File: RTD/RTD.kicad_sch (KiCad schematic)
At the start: 48 parts, among them SW1 SW_SPDT, U1 THVD1420D, U2 STM32F103C8Tx

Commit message: light refactor
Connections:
- net -24V: now also SDT1.2 (-VIN); no longer SDT1. (-VIN)
- net 24V: now also SDT1.1 (+VIN); no longer SDT1. (-VIN)
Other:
- moved on the sheet: C1, C4, Debug_power1, Debugger1, F1, L1, L2, Pwr_term1

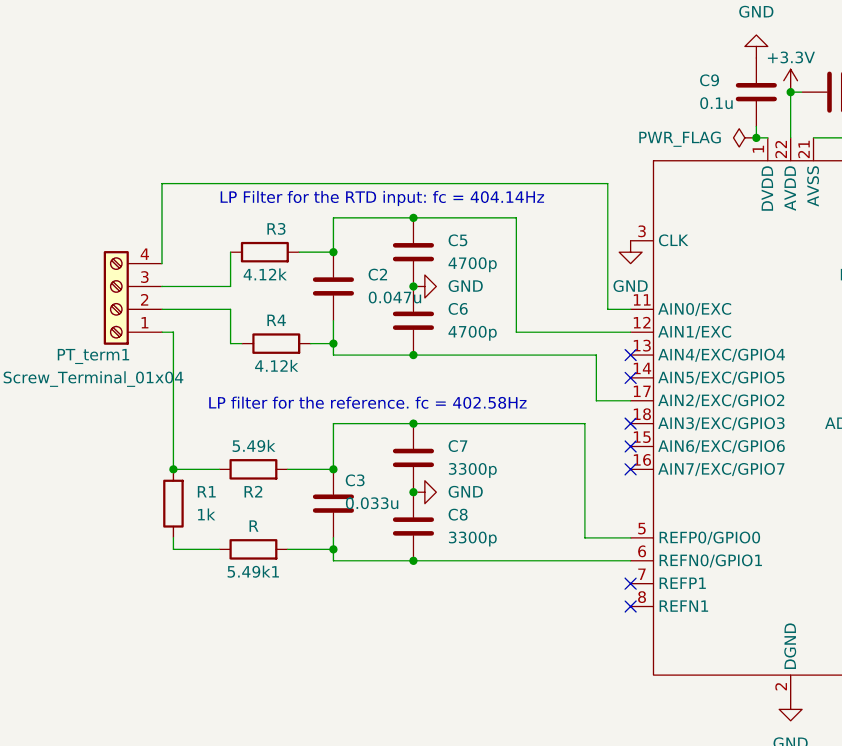
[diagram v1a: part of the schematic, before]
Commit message: fix: changes value in LP filters
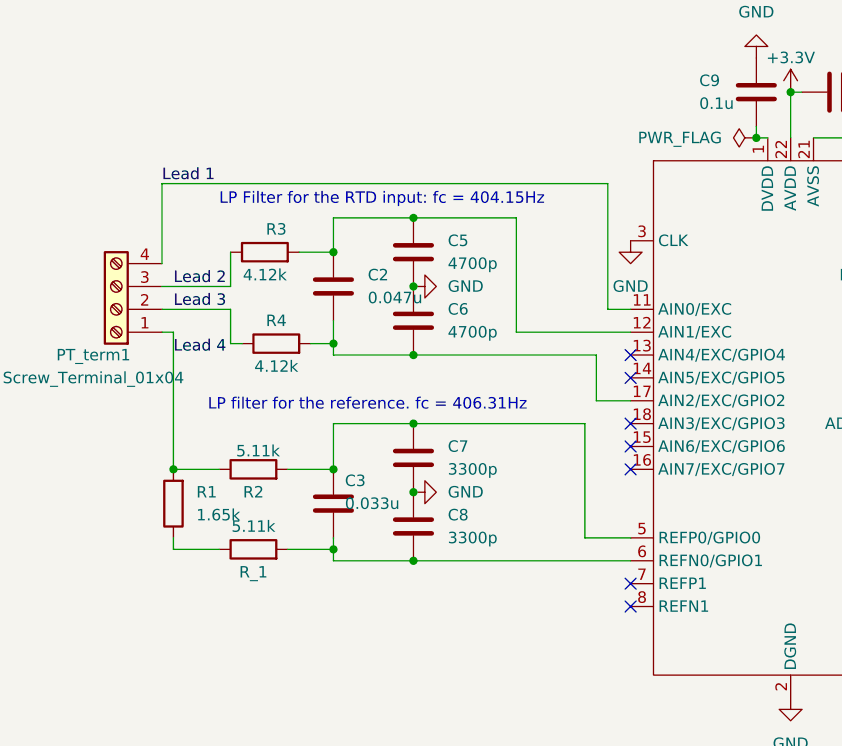
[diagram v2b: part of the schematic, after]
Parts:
- R1: value 1k -> 1.65k
- R2: value 5.49k -> 5.11k
- R_1: renamed from 5.49k1; value R -> 5.11k
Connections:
- net Lead 4: now reaches PT_term1.1 (Pin_1), R1.2, R2.1
- net Lead 3: now reaches PT_term1.2 (Pin_2), R4.1
- net Lead 1: now reaches ADS1.11 (AIN0/EXC), PT_term1.4 (Pin_4)
- net Lead 2: now reaches PT_term1.3 (Pin_3), R3.1
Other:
- note added: "LP Filter for the RTD input: fc = 404.15Hz"
- note added: "LP filter for the reference. fc = 406.31Hz"
- note removed: "LP Filter for the RTD input: fc = 404.14Hz"
- note removed: "LP filter for the reference. fc = 402.58Hz"
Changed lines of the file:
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@@
 		)
 	)
-	(text "LP filter for the reference. fc = 402.58Hz"
+	(text "LP filter for the reference. fc = 406.31Hz"
 		(exclude_from_sim no)
 		(at 43.18 66.04 0)
@@
 		)
 	)
-	(text "LP Filter for the RTD input: fc = 404.14Hz"
+	(text "LP Filter for the RTD input: fc = 404.15Hz"
 		(exclude_from_sim no)
 		(at 44.45 43.18 0)
@@
 		)
 	)
+	(label "Lead 3"
+		(at 39.37 54.61 0)
+		(effects
+			(font
+				(size 1.27 1.27)
+			)
+			(justify left bottom)
+		)
+	)
+	(label "Lead 4"
+		(at 39.37 59.69 0)
+		(effects
+			(font
+				(size 1.27 1.27)
+			)
+			(justify left bottom)
+		)
+	)
 	(label "-24V"
 		(at 62.23 139.7 270)
@@
 		)
 	)
+	(label "Lead 2"
+		(at 39.37 52.07 0)
+		(effects
+			(font
+				(size 1.27 1.27)
+			)
+			(justify left bottom)
+		)
+	)
 	(label "B"
 		(at 130.81 130.81 0)
@@
 		)
 	)
+	(label "Lead 1"
+		(at 38.1 40.64 0)
+		(effects
+			(font
+				(size 1.27 1.27)
+			)
+			(justify left bottom)
+		)
+	)
 	(label "BOOT0"
 		(at 214.63 46.99 0)
@@
 			)
 		)
-		(property "Value" "5.49k"
-			(at 48.26 69.85 90)
+		(property "Value" "5.11k"
+			(at 48.768 70.358 90)
 			(effects
 				(font
@@
 			)
 		)
-		(property "Value" "1k"
+		(property "Value" "1.65k"
 			(at 41.91 77.47 0)
 			(effects
@@
 		(on_board yes)
 		(dnp no)
-		(property "Reference" "5.49k1"
+		(property "Reference" "R_1"
 			(at 48.26 83.82 90)
 			(effects
@@
 			)
 		)
-		(property "Value" "R"
+		(property "Value" "5.11k"
 			(at 48.26 78.74 90)
 			(effects
@@
 			(project "RTD"
 				(path "/b0f0ce8f-6820-44a1-a501-600cf997055b"
-					(reference "5.49k1")
+					(reference "R_1")
 					(unit 1)
 				)
